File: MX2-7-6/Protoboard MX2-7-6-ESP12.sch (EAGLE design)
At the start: 52 parts

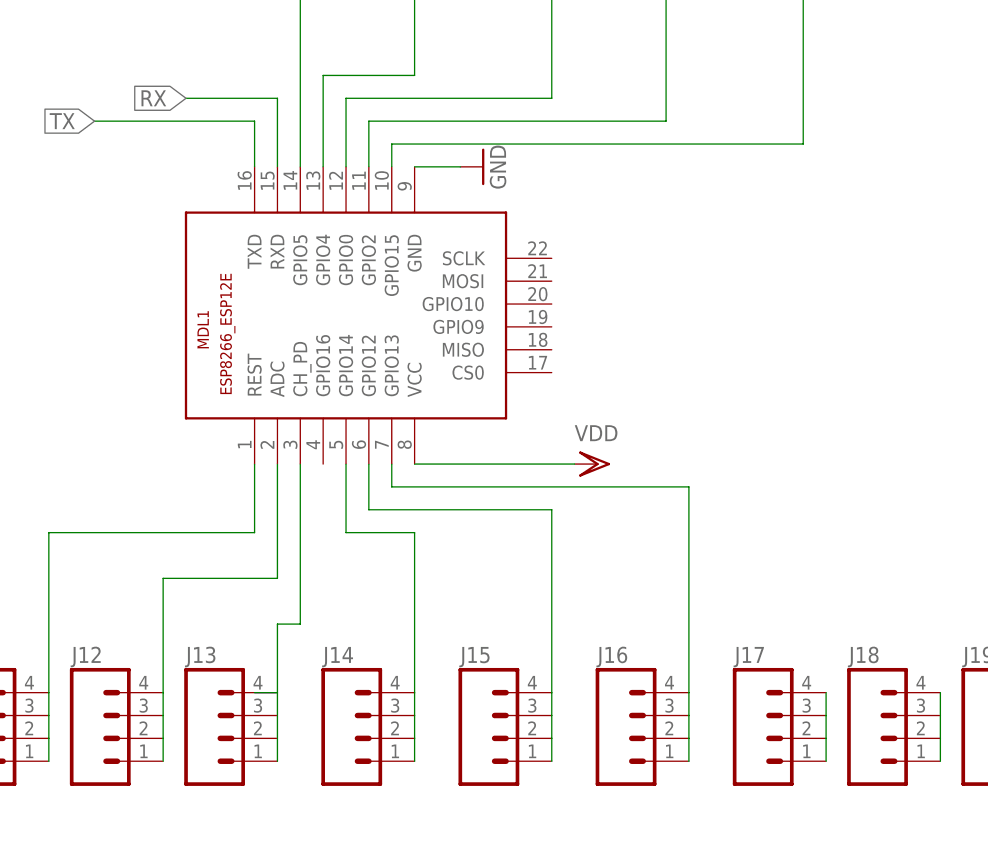
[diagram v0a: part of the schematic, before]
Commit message: Change ESP Module
Changed to Device/Package Adafruit uses
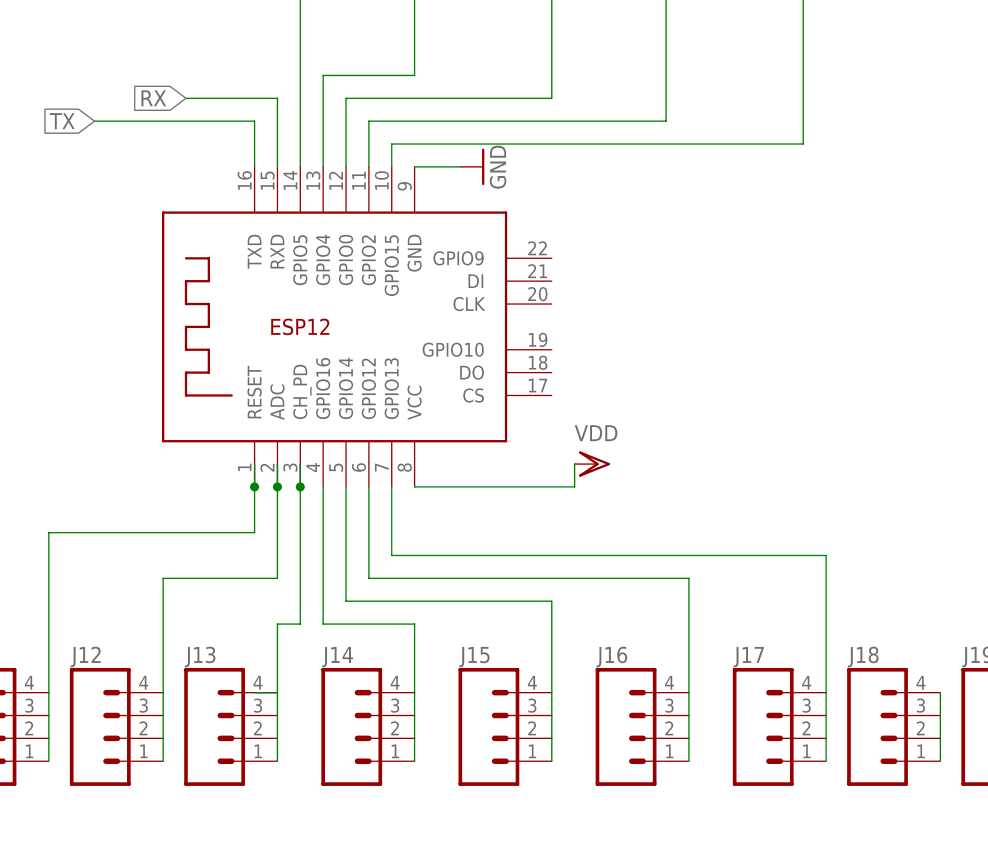
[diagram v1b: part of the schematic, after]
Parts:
- removed MDL1: (no value), ESP8266-ESP12E:ESP8266-12EESP8266-ESP12E
- added X1: ESP-12E, microbuilder:ESP-12E
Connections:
- removed net N$26: J14.1, J14.2, J14.3, J14.4, MDL1.GPIO14
- removed net N$55: J15.1, J15.2, J15.3, J15.4, MDL1.GPIO12
- removed net N$56: J16.1, J16.2, J16.3, J16.4, MDL1.GPIO13
- new net N$2: J16.1, J16.2, J16.3, J16.4, X1.GPIO12
- new net N$36: J14.1, J14.2, J14.3, J14.4, X1.GPIO16
- new net N$6: J15.1, J15.2, J15.3, J15.4, X1.GPIO14
- net GND: now also X1.GND; no longer MDL1.GND
- net N$10: now also X1.GPIO4; no longer MDL1.GPIO4
- net N$11: now also X1.GPIO0; no longer MDL1.GPIO0
- net N$12: now also X1.GPIO2; no longer MDL1.GPIO2
- net N$13: now also X1.GPIO15; no longer MDL1.GPIO15
- net N$34: now also X1.GPIO13
- net N$50: now also X1.RESET; no longer MDL1.REST
- net N$51: now also X1.ADC; no longer MDL1.ADC
- net N$52: now also X1.CH_PD; no longer MDL1.CH_PD
- net N$9: now also X1.GPIO5; no longer MDL1.GPIO5
- net RX: now also X1.RXD; no longer MDL1.RXD
- net TX: now also X1.TXD; no longer MDL1.TXD
- net VDD: now also X1.VCC; no longer MDL1.VCC

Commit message: update and and 3.3V label
Update labels
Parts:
- VDD: value (none) -> GND
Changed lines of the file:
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@@
 <part name="GND8" library="supply1" deviceset="GND" device=""/>
 <part name="VDD5" library="supply1" deviceset="VDD" device=""/>
-<part name="VDD" library="SparkFun-Connectors" deviceset="M19" device="1X19_NO_SILK"/>
+<part name="VDD" library="SparkFun-Connectors" deviceset="M19" device="1X19_NO_SILK" value="GND"/>
 <part name="3.3V" library="SparkFun-Connectors" deviceset="M19" device="1X19_NO_SILK"/>
 <part name="VDD2" library="supply1" deviceset="VDD" device=""/>

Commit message: Routed
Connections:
- removed net N$7: J1.1, J1.2, J1.3, J1.4
- removed net N$8: J2.1, J2.2, J2.3, J2.4
- net RX: now also J2.1, J2.2, J2.3, J2.4
- net TX: now also J1.1, J1.2, J1.3, J1.4
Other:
- moved on the sheet: J1, J2
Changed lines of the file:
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@@
 <?xml version="1.0" encoding="utf-8"?>
 <!DOCTYPE eagle SYSTEM "eagle.dtd">
-<eagle version="7.7.0">
+<eagle version="7.6.0">
 <drawing>
 <settings>
@@
 <instance part="J7" gate="G$1" x="170.18" y="93.98"/>
 <instance part="J8" gate="G$1" x="185.42" y="93.98"/>
-<instance part="J1" gate="G$1" x="200.66" y="93.98"/>
-<instance part="J2" gate="G$1" x="213.36" y="93.98"/>
+<instance part="J1" gate="G$1" x="88.9" y="93.98"/>
+<instance part="J2" gate="G$1" x="101.6" y="93.98"/>
 <instance part="J9" gate="G$1" x="226.06" y="93.98"/>
 <instance part="J10" gate="G$1" x="238.76" y="93.98"/>
@@
 <label x="96.52" y="58.42" size="1.778" layer="95" rot="R180" xref="yes"/>
 <pinref part="X1" gate="G$1" pin="TXD"/>
+<pinref part="J1" gate="G$1" pin="4"/>
+<pinref part="J1" gate="G$1" pin="3"/>
+<wire x1="93.98" y1="99.06" x2="93.98" y2="96.52" width="0.1524" layer="91"/>
+<pinref part="J1" gate="G$1" pin="2"/>
+<wire x1="93.98" y1="96.52" x2="93.98" y2="93.98" width="0.1524" layer="91"/>
+<pinref part="J1" gate="G$1" pin="1"/>
+<wire x1="93.98" y1="93.98" x2="93.98" y2="91.44" width="0.1524" layer="91"/>
+<wire x1="93.98" y1="91.44" x2="93.98" y2="83.82" width="0.1524" layer="91"/>
+<wire x1="93.98" y1="83.82" x2="114.3" y2="83.82" width="0.1524" layer="91"/>
+<wire x1="114.3" y1="83.82" x2="114.3" y2="58.42" width="0.1524" layer="91"/>
+<junction x="114.3" y="58.42"/>
 </segment>
 <segment>
@@
 <label x="106.68" y="60.96" size="1.778" layer="95" rot="R180" xref="yes"/>
 <pinref part="X1" gate="G$1" pin="RXD"/>
+<pinref part="J2" gate="G$1" pin="1"/>
+<pinref part="J2" gate="G$1" pin="2"/>
+<wire x1="106.68" y1="91.44" x2="106.68" y2="93.98" width="0.1524" layer="91"/>
+<pinref part="J2" gate="G$1" pin="3"/>
+<wire x1="106.68" y1="93.98" x2="106.68" y2="96.52" width="0.1524" layer="91"/>
+<pinref part="J2" gate="G$1" pin="4"/>
+<wire x1="106.68" y1="96.52" x2="106.68" y2="99.06" width="0.1524" layer="91"/>
+<wire x1="106.68" y1="91.44" x2="106.68" y2="86.36" width="0.1524" layer="91"/>
+<wire x1="106.68" y1="86.36" x2="116.84" y2="86.36" width="0.1524" layer="91"/>
+<wire x1="116.84" y1="86.36" x2="116.84" y2="60.96" width="0.1524" layer="91"/>
+<junction x="116.84" y="60.96"/>
 </segment>
 <segment>
@@
 </segment>
 </net>
-<net name="N$7" class="0">
-<segment>
-<pinref part="J1" gate="G$1" pin="4"/>
-<pinref part="J1" gate="G$1" pin="3"/>
-<wire x1="205.74" y1="99.06" x2="205.74" y2="96.52" width="0.1524" layer="91"/>
-<pinref part="J1" gate="G$1" pin="2"/>
-<wire x1="205.74" y1="96.52" x2="205.74" y2="93.98" width="0.1524" layer="91"/>
-<pinref part="J1" gate="G$1" pin="1"/>
-<wire x1="205.74" y1="93.98" x2="205.74" y2="91.44" width="0.1524" layer="91"/>
-</segment>
-</net>
-<net name="N$8" class="0">
-<segment>
-<pinref part="J2" gate="G$1" pin="1"/>
-<pinref part="J2" gate="G$1" pin="2"/>
-<wire x1="218.44" y1="91.44" x2="218.44" y2="93.98" width="0.1524" layer="91"/>
-<pinref part="J2" gate="G$1" pin="3"/>
-<wire x1="218.44" y1="93.98" x2="218.44" y2="96.52" width="0.1524" layer="91"/>
-<pinref part="J2" gate="G$1" pin="4"/>
-<wire x1="218.44" y1="96.52" x2="218.44" y2="99.06" width="0.1524" layer="91"/>
-</segment>
-</net>
